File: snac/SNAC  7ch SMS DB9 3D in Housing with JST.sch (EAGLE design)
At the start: 45 parts, among them IC1 4030D, IC2 MAX660CPACS, Q1 BSS138, Q2 BSS138, Q3 BSS138, Q4 BSS138, Q5 BSS138, Q6 BSS138, Q7 BSS138, Q8 BSS138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

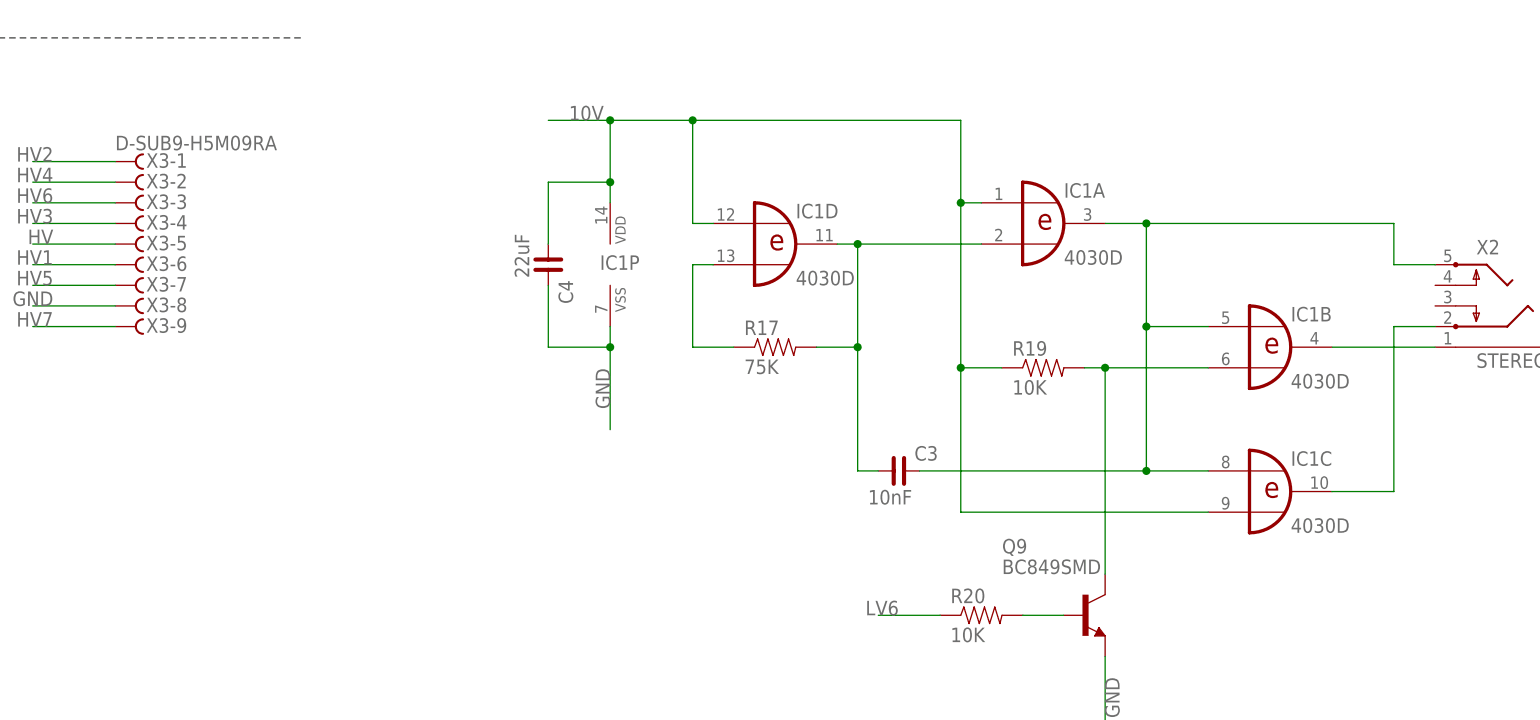
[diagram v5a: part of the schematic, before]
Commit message: XOR Osc on 3D boards needed an extra resistor
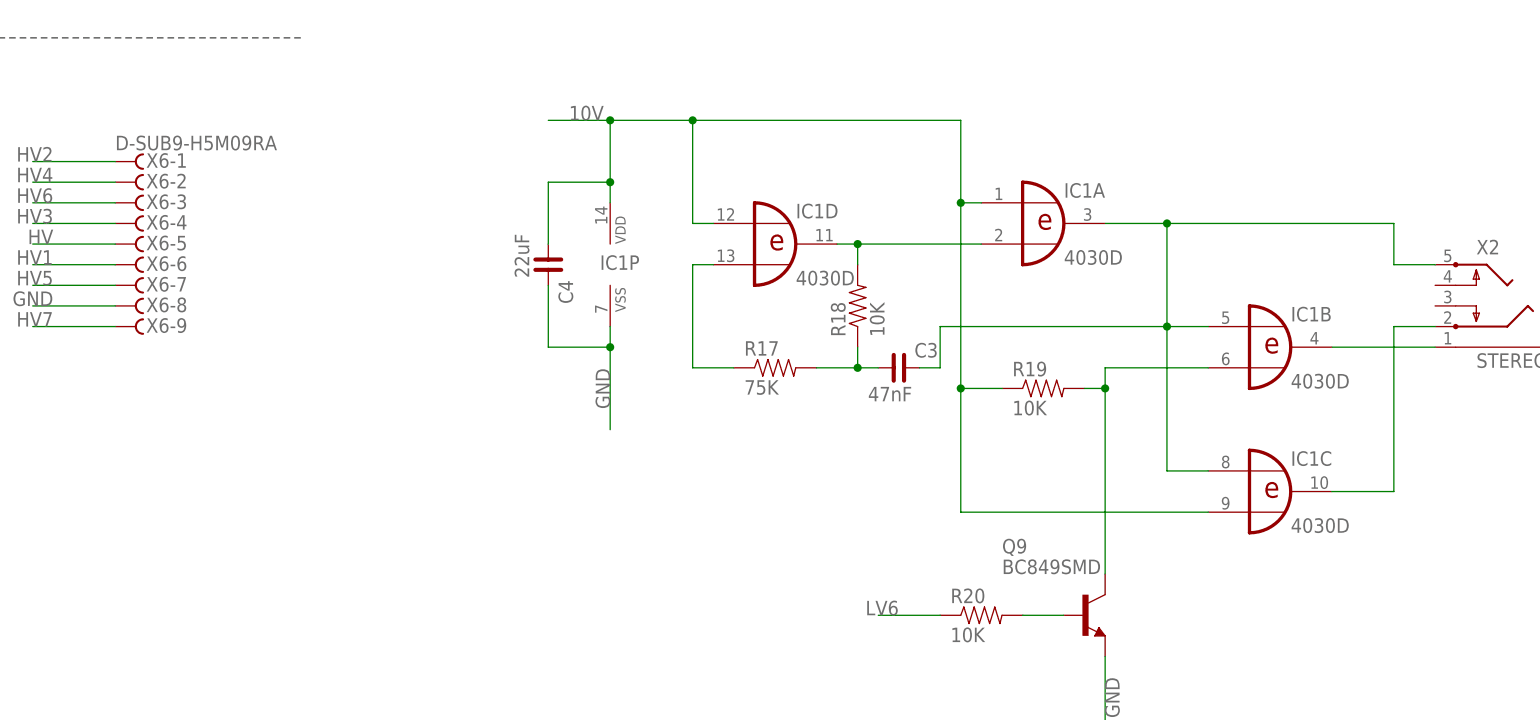
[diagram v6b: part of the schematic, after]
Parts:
- added R18: 10K, SparkFun:RESISTOR0603-RES
- C3: value 10nF -> 47nF
- renumbered X3 to X6
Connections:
- new net N$24: C3.1, R17.2, R18.1
- net N$5: now also R18.2; no longer C3.1, R17.2
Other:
- moved on the sheet: C3, R17, R19

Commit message: fixed major screw-up with the USERIO/JST pinout. Removed the unused FET
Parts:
- removed Q8: BSS138, SparkFun:MOSFET-NCHANNELSMD
- removed R15, R16: 10K, SparkFun:RESISTOR0603-RES
- removed X1: JST-XH-02-PIN-ROUND-PAD, Rembrandt Electronics - JST XH Connectors v1-0:JST-XH-02-PIN-ROUND-PAD
- U1: value PMIC-LDO-XC6206P332MR-G(SOT23) -> AP2127N-3.3TRG1
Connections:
- removed net HV8: Q8.D, R16.2
- removed net LV8: Q8.S, R15.2, X1-2.S
- net HV: no longer R16.1
- net J1: now also X4-5.S, X5-5.S; no longer X4-9.S, X5-9.S
- net LV: no longer Q8.G, R15.1
- net LV1: now also X4-6.S, X5-6.S; no longer X4-8.S, X5-8.S
- net LV2: now also X4-3.S, X5-3.S; no longer X4-2.S, X5-2.S
- net LV4: now also X4-2.S, X5-2.S; no longer X4-3.S, X5-3.S
- net LV5: now also X4-8.S, X5-8.S; no longer X4-6.S, X5-6.S
- net LV6: now also X4-9.S, X5-9.S; no longer X4-5.S, X5-5.S
- net LV7: no longer X1-1.S
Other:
- note added: ""USB 3.0" (SOCKET!)..."
- note added: "(IOB P6)"
- note added: "1."
- note added: "15+19. GND"
- note added: "16+18. 5V"
- note added: "17. 3V3"
- note added: "2."
- note added: "3."
- note added: "4."
- note added: "5."
- note added: "6."
- note added: "7. (via jumper)"
- note added: "<- Older SDRAM board"
- note added: "Arduino_IO0"
- note added: "Arduino_IO1"
- note added: "Arduino_IO2"
- note added: "Arduino_IO3"
- note added: "Arduino_IO4"
- note added: "Arduino_IO5"
- note added: "Arduino_IO6"
- note added: "Arduino_IO7"
- note added: "Arduino_RST"
- note added: "CKE"
- note added: "DH"
- note added: "DIG_MCP_SCL"
- note added: "DIG_MCP_SDA"
- note added: "DIG_SD_CLK"
- note added: "DIG_SD_MISO"
- note added: "DIG_SD_MOSI"
- note added: "DL"
- note added: "JP3 PIN1"
- note added: "JP3 PIN2"
- note added: "JP3 PIN3"
- note added: "JP3 PIN4"
- note added: "JP3 PIN5"
- note added: "JP3 PIN6"
- note added: "JP3 PIN7"
- note added: "JP3 PIN8"
- note added: "JP5 PIN1"
- note added: "JP5 PIN2"
- note added: "JP5 PIN3"
- note added: "JP5 PIN4"
- note added: "JP5 PIN5"
- note added: "JP5 PIN6"
- note added: "JP5 PIN7"
- note added: "JP5 PIN8"
- note added: "LV1"
- note added: "LV2"
- note added: "LV3"
- note added: "LV4"
- note added: "LV5"
- note added: "LV6"
- note added: "LV7"
- note added: "Note: Pin mapping FIXED, vs the first Jammix prototype!"
- note added: "Note: Pin mapping FIXED, vs the first prototype!"
- note added: "P6"
- note added: "P7"
- note added: "PIN_AF13"
- note added: "PIN_AG10"
- note added: "PIN_AG13"
- note added: "PIN_AG8"
- note added: "PIN_AG9"
- note added: "PIN_AH7"
- note added: "PIN_AH8"
- note added: "PIN_U13"
- note added: "PIN_U14"
- note added: "SNAC NAME"
- note added: "SNAC/Bliss HDMI..."
- note added: "USER_PORT..."
- note added: "digikey AP2127N-3.3TRG1DICT-ND"
- note removed: ""USB 3.0" SKT..."
- note removed: "IOB NAME..."
- note removed: "USERIO NAME..."
- note removed: "USERIO_LV1"
- note removed: "USERIO_LV2"
- note removed: "USERIO_LV3"
- note removed: "USERIO_LV4"
- note removed: "USERIO_LV5"
- note removed: "USERIO_LV6"
- note removed: "USERIO_LV7"
- moved on the sheet: X4-1, X4-2, X4-3, X4-4, X4-5, X4-6, X4-7, X4-8, X4-9, X5-1, X5-2, X5-3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

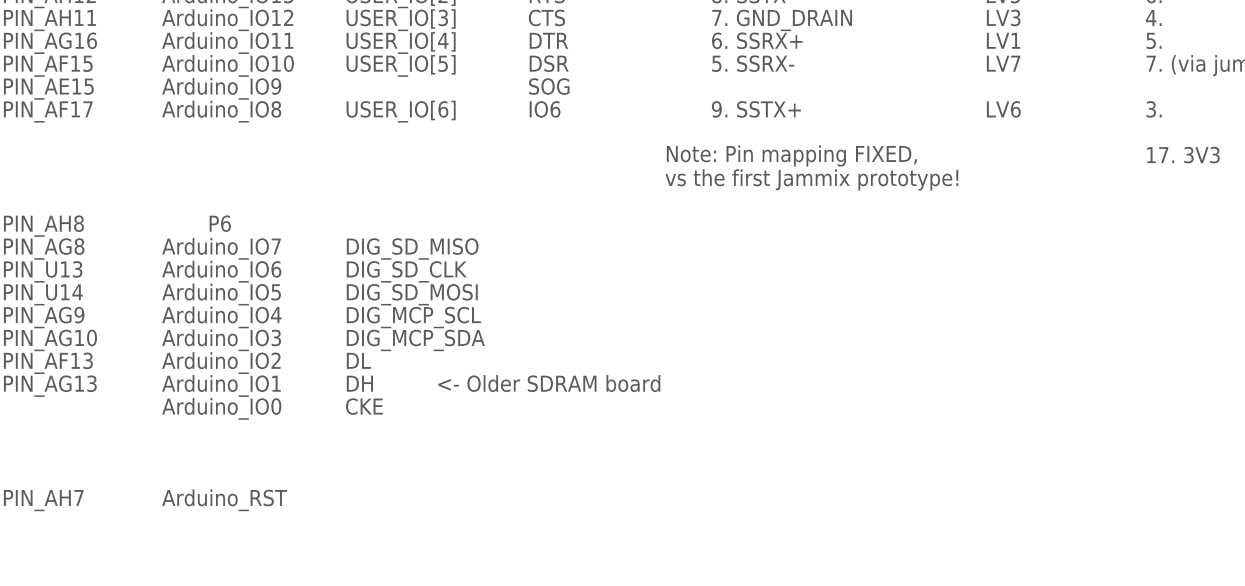
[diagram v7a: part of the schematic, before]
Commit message: slight tidy of SMS DB9 3D board
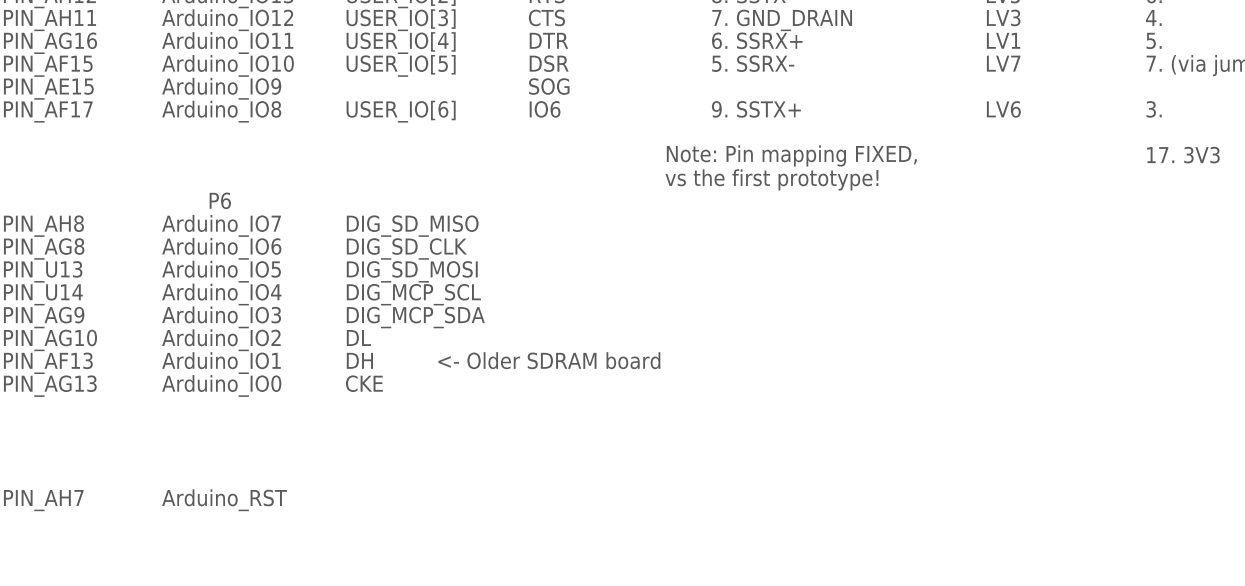
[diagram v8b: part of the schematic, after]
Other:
- note removed: "Note: Pin mapping FIXED, vs the first Jammix prototype!"
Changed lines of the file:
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@@
 <text x="332.74" y="223.52" size="1.778" layer="97">Arduino_IO9</text>
 <text x="332.74" y="220.98" size="1.778" layer="97">Arduino_IO8</text>
-<text x="332.74" y="205.74" size="1.778" layer="97">Arduino_IO7</text>
-<text x="332.74" y="203.2" size="1.778" layer="97">Arduino_IO6</text>
-<text x="332.74" y="200.66" size="1.778" layer="97">Arduino_IO5</text>
-<text x="332.74" y="198.12" size="1.778" layer="97">Arduino_IO4</text>
-<text x="332.74" y="195.58" size="1.778" layer="97">Arduino_IO3</text>
-<text x="332.74" y="193.04" size="1.778" layer="97">Arduino_IO2</text>
-<text x="332.74" y="190.5" size="1.778" layer="97">Arduino_IO1</text>
-<text x="332.74" y="187.96" size="1.778" layer="97">Arduino_IO0</text>
+<text x="332.74" y="208.28" size="1.778" layer="97">Arduino_IO7</text>
+<text x="332.74" y="205.74" size="1.778" layer="97">Arduino_IO6</text>
+<text x="332.74" y="203.2" size="1.778" layer="97">Arduino_IO5</text>
+<text x="332.74" y="200.66" size="1.778" layer="97">Arduino_IO4</text>
+<text x="332.74" y="198.12" size="1.778" layer="97">Arduino_IO3</text>
+<text x="332.74" y="195.58" size="1.778" layer="97">Arduino_IO2</text>
+<text x="332.74" y="193.04" size="1.778" layer="97">Arduino_IO1</text>
+<text x="332.74" y="190.5" size="1.778" layer="97">Arduino_IO0</text>
 <text x="373.38" y="243.84" size="1.778" layer="97">RX</text>
 <text x="373.38" y="241.3" size="1.778" layer="97">TX</text>
@@
 <text x="373.38" y="251.46" size="1.778" layer="97">USER_PORT...</text>
 <text x="332.74" y="236.22" size="1.778" layer="97">GND</text>
-<text x="353.06" y="193.04" size="1.778" layer="97">DL</text>
-<text x="353.06" y="190.5" size="1.778" layer="97">DH</text>
-<text x="353.06" y="187.96" size="1.778" layer="97">CKE</text>
-<text x="363.22" y="190.5" size="1.778" layer="97">&lt;- Older SDRAM board</text>
+<text x="353.06" y="195.58" size="1.778" layer="97">DL</text>
+<text x="353.06" y="193.04" size="1.778" layer="97">DH</text>
+<text x="353.06" y="190.5" size="1.778" layer="97">CKE</text>
+<text x="363.22" y="193.04" size="1.778" layer="97">&lt;- Older SDRAM board</text>
 <text x="393.7" y="241.3" size="1.778" layer="97">2. D-</text>
 <text x="393.7" y="243.84" size="1.778" layer="97">3. D+</text>
@@
 <text x="441.96" y="251.46" size="1.778" layer="97">SNAC/Bliss HDMI...</text>
 <text x="441.96" y="215.9" size="1.778" layer="97">17. 3V3</text>
-<text x="353.06" y="205.74" size="1.778" layer="97">DIG_SD_MISO</text>
-<text x="353.06" y="203.2" size="1.778" layer="97">DIG_SD_CLK</text>
-<text x="353.06" y="200.66" size="1.778" layer="97">DIG_SD_MOSI</text>
-<text x="353.06" y="198.12" size="1.778" layer="97">DIG_MCP_SCL</text>
-<text x="353.06" y="195.58" size="1.778" layer="97">DIG_MCP_SDA</text>
+<text x="353.06" y="208.28" size="1.778" layer="97">DIG_SD_MISO</text>
+<text x="353.06" y="205.74" size="1.778" layer="97">DIG_SD_CLK</text>
+<text x="353.06" y="203.2" size="1.778" layer="97">DIG_SD_MOSI</text>
+<text x="353.06" y="200.66" size="1.778" layer="97">DIG_MCP_SCL</text>
+<text x="353.06" y="198.12" size="1.778" layer="97">DIG_MCP_SDA</text>
 <text x="353.06" y="251.46" size="1.778" layer="97">Core name...</text>
 <text x="353.06" y="220.98" size="1.778" layer="97">USER_IO[6]</text>
@@
 <text x="353.06" y="243.84" size="1.778" layer="97">USER_IO[0]</text>
 <text x="337.82" y="246.38" size="1.778" layer="97">P7</text>
-<text x="337.82" y="208.28" size="1.778" layer="97">P6</text>
+<text x="337.82" y="210.82" size="1.778" layer="97">P6</text>
 <text x="314.96" y="220.98" size="1.778" layer="97">PIN_AF17</text>
 <text x="314.96" y="226.06" size="1.778" layer="97">PIN_AF15</text>
@@
 <text x="424.18" y="220.98" size="1.778" layer="97">LV6</text>
 <text x="388.62" y="213.36" size="1.778" layer="97">Note: Pin mapping FIXED,
-vs the first Jammix prototype!</text>
+vs the first prototype!</text>
 <text x="30.48" y="86.36" size="1.778" layer="97">Note: Pin mapping FIXED,
 vs the first prototype!</text>
